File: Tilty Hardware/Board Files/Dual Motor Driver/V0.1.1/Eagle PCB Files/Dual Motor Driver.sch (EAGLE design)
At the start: 33 parts, among them J1 AVR_SPI_PRG_6PTH, Q1 16MHz, U1 ATMEGA328P, U2 L298_BRIDGE_DRIVER, U5 VOLTAGE-REGULATOR

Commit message: Tilty PCB work
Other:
- note added: "headers need to be updated!"
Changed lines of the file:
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@@
 <text x="2.54" y="5.08" size="1.778" layer="91">Change to a non-
 Sparkfun button</text>
+<text x="182.88" y="40.64" size="2.54" layer="91" ratio="15">headers need to be updated!</text>
 </plain>
 <instances>

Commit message: Finished Tilty Duo/Quad 0.2.4, work on motor driver
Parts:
- removed JP8: (no value), SparkFun-Connectors:M063.5MM-6
- removed JP9: (no value), pinhead:PINHD-2X3/90
- removed U5: VOLTAGE-REGULATOR, My Parts:VOLTAGE-REGULATOR
- added U3: LM2931, on-semiconductor:LM2931
- C6: value 0.1uF -> 4.7uF
- C7: value 1uF -> 0.1uF
- JP7: value (none) -> 2-POS_SMD_TERM_BLOCK; device pinhead:PINHD-2X3/90 -> My Parts:2-POS_SMD_TERM_BLOCK
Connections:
- net +24V: now also JP7.1, U3.VIN; no longer JP8.4, U5.VIN
- net +5V: now also U3.5V; no longer U5.VOUT
- net ENC1B: now also U1.PC1(ADC1)
- net ENC2A: now also JP5.3, U1.PC0(ADC0); no longer JP5.4, U1.PD3(INT1)
- net ENC2B: now also JP5.4, U1.PD3(INT1); no longer JP5.3
- net GND: now also JP7.2, U3.GND; no longer JP8.3, U5.GND
- net M1A: now also JP6.2; no longer JP6.1, JP8.6
- net M1B: now also JP6.1; no longer JP6.2, JP8.5
- net M2A: now also JP5.6; no longer JP5.5, JP8.2
- net M2B: now also JP5.5; no longer JP5.6, JP8.1
- net SENSE_1: now also U1.PC2(ADC2); no longer U1.PC0(ADC0)
- net SENSE_2: now also U1.PC3(ADC3); no longer U1.PC1(ADC1)

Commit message: Nearly finalized dual motor driver add-on
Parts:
- added D10: (no value), SparkFun-LED:LED-GREENLED-0805_NO_SILK
- added D9: (no value), diode:DIODE-DO214AA
- added JP10, JP9: (no value), SparkFun-Connectors:M02PTH
- added JP8: (no value), SparkFun-Connectors:M04LOCK
- added R6: (no value), resistor:R-US_R0603
- added SJ2: SOLDERJUMPERTRACE, SparkFun-Passives:SOLDERJUMPERTRACE
- JP1, JP2, JP3, JP4: value (none) -> 8-PIN_HEADER; device pinhead:PINHD-1X81X08_NO_SILK -> My Parts:8-PIN_HEADER
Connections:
- new net N$1: D10.A, R6.2
- new net N$3: C7.1, D9.A, SJ2.1, U3.VIN
- new net RX: JP8.3, U1.PD0(RXD)
- new net TX: JP8.4, U1.PD1(TXD)
- net +24V: now also D9.C, SJ2.2; no longer C7.1, U3.VIN
- net +5V: now also JP8.1, R6.1
- net GND: now also D10.C, JP8.2, U2.GND@20
- net M1A: now also JP9.2
- net M1B: now also JP9.1
- net M2A: now also JP10.2
- net M2B: now also JP10.1
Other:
- note added: "Zener"
- note removed: "headers need to be updated!"

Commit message: New RC Receiver add-on testing code and minor motor driver updates
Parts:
- J1: value AVR_SPI_PRG_6PTH -> AVR_SPI_PRG_62X3_LOCK; device SparkFun-Connectors:AVR_SPI_PRG_6PTH -> SparkFun-Connectors:AVR_SPI_PRG_62X3_LOCK
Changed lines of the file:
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@@
 </part>
 <part name="P+4" library="supply1" deviceset="+24V" device=""/>
-<part name="J1" library="SparkFun-Connectors" deviceset="AVR_SPI_PRG_6" device="PTH"/>
+<part name="J1" library="SparkFun-Connectors" deviceset="AVR_SPI_PRG_6" device="2X3_LOCK" value="AVR_SPI_PRG_62X3_LOCK"/>
 <part name="GND6" library="supply1" deviceset="GND" device=""/>
 <part name="P+5" library="supply1" deviceset="+5V" device=""/>

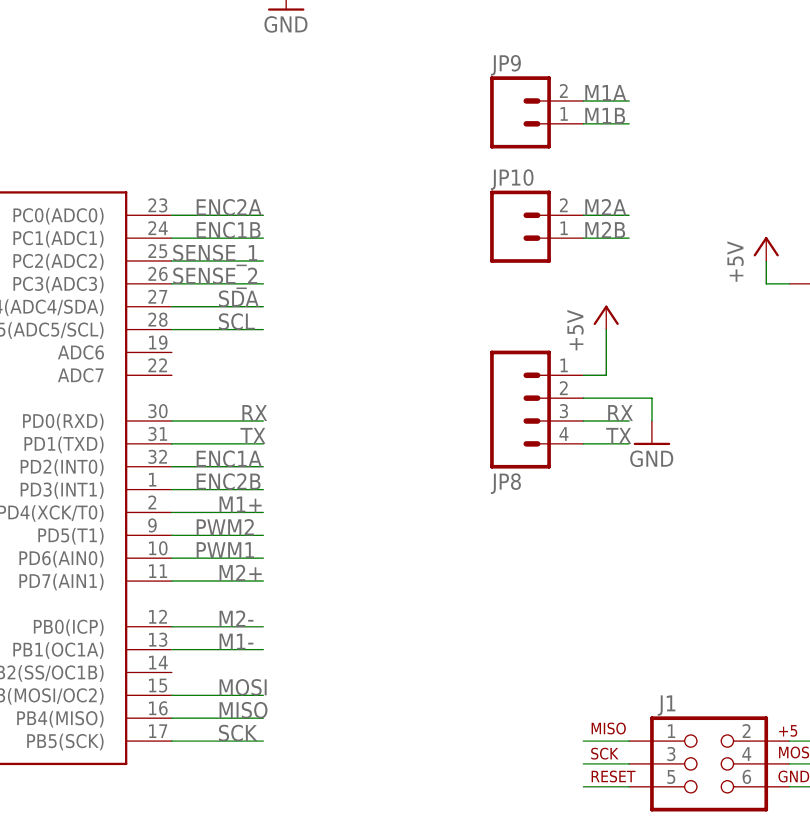
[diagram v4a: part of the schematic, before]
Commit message: Motor driver: added test code, updated things.todo, some hardware updates
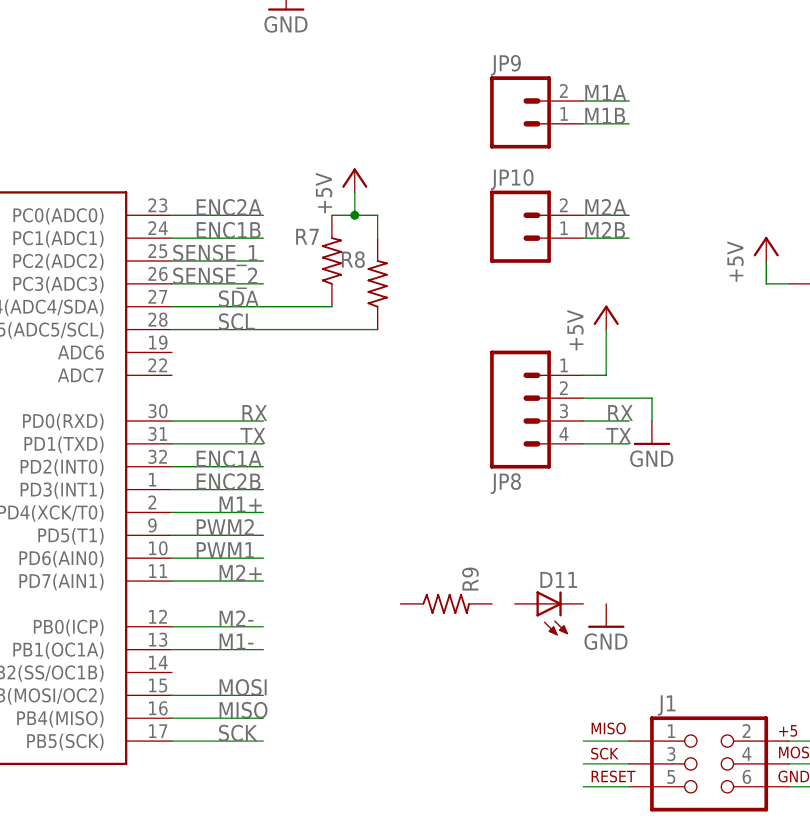
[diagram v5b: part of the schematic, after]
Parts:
- added D11: (no value), SparkFun-LED:LED-GREENLED-0805_NO_SILK
- added R7, R8, R9: (no value), resistor:R-US_R0603
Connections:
- net +5V: now also R7.2, R8.2
- net SCL: now also R8.1
- net SDA: now also R7.1
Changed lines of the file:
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@@
 <part name="P+13" library="supply1" deviceset="+5V" device=""/>
 <part name="GND16" library="supply1" deviceset="GND" device=""/>
+<part name="R7" library="resistor" deviceset="R-US_" device="R0603"/>
+<part name="R8" library="resistor" deviceset="R-US_" device="R0603"/>
+<part name="P+14" library="supply1" deviceset="+5V" device=""/>
+<part name="R9" library="resistor" deviceset="R-US_" device="R0603"/>
+<part name="D11" library="SparkFun-LED" deviceset="LED-GREEN" device="LED-0805_NO_SILK"/>
+<part name="GND17" library="supply1" deviceset="GND" device=""/>
 </parts>
 <sheets>
@@
 <instance part="P+13" gate="1" x="167.64" y="63.5"/>
 <instance part="GND16" gate="1" x="190.5" y="53.34"/>
+<instance part="R7" gate="G$1" x="119.38" y="60.96" smashed="yes" rot="R90">
+<attribute name="NAME" x="118.11" y="64.5414" size="1.778" layer="95" rot="R180"/>
+<attribute name="VALUE" x="118.11" y="61.722" size="1.778" layer="96" rot="R180"/>
+</instance>
+<instance part="R8" gate="G$1" x="124.46" y="58.42" smashed="yes" rot="R90">
+<attribute name="NAME" x="123.19" y="62.0014" size="1.778" layer="95" rot="R180"/>
+<attribute name="VALUE" x="123.19" y="59.182" size="1.778" layer="96" rot="R180"/>
+</instance>
+<instance part="P+14" gate="1" x="121.92" y="71.12"/>
+<instance part="R9" gate="G$1" x="132.08" y="22.86" smashed="yes">
+<attribute name="NAME" x="135.6614" y="24.13" size="1.778" layer="95" rot="R90"/>
+<attribute name="VALUE" x="132.842" y="24.13" size="1.778" layer="96" rot="R90"/>
+</instance>
+<instance part="D11" gate="G$1" x="142.24" y="22.86" rot="R90"/>
+<instance part="GND17" gate="1" x="149.86" y="20.32"/>
 </instances>
 <busses>
@@
 <wire x1="167.64" y1="58.42" x2="170.18" y2="58.42" width="0.1524" layer="91"/>
 </segment>
+<segment>
+<pinref part="R7" gate="G$1" pin="2"/>
+<pinref part="R8" gate="G$1" pin="2"/>
+<wire x1="119.38" y1="66.04" x2="121.92" y2="66.04" width="0.1524" layer="91"/>
+<wire x1="121.92" y1="66.04" x2="124.46" y2="66.04" width="0.1524" layer="91"/>
+<wire x1="124.46" y1="66.04" x2="124.46" y2="63.5" width="0.1524" layer="91"/>
+<pinref part="P+14" gate="1" pin="+5V"/>
+<wire x1="121.92" y1="68.58" x2="121.92" y2="66.04" width="0.1524" layer="91"/>
+<junction x="121.92" y="66.04"/>
+</segment>
 </net>
 <net name="RESET" class="0">
@@
 <segment>
 <pinref part="U1" gate="G$1" pin="PC4(ADC4/SDA)"/>
-<wire x1="101.6" y1="55.88" x2="111.76" y2="55.88" width="0.1524" layer="91"/>
+<wire x1="101.6" y1="55.88" x2="119.38" y2="55.88" width="0.1524" layer="91"/>
 <label x="106.68" y="55.88" size="1.778" layer="95"/>
+<pinref part="R7" gate="G$1" pin="1"/>
 </segment>
 </net>
@@
 <segment>
 <pinref part="U1" gate="G$1" pin="PC5(ADC5/SCL)"/>
-<wire x1="101.6" y1="53.34" x2="111.76" y2="53.34" width="0.1524" layer="91"/>
 <label x="106.68" y="53.34" size="1.778" layer="95"/>
-</segment>
-</net>
+<pinref part="R8" gate="G$1" pin="1"/>
+<wire x1="101.6" y1="53.34" x2="124.46" y2="53.34" width="0.1524" layer="91"/>
+</segment>
+</net>

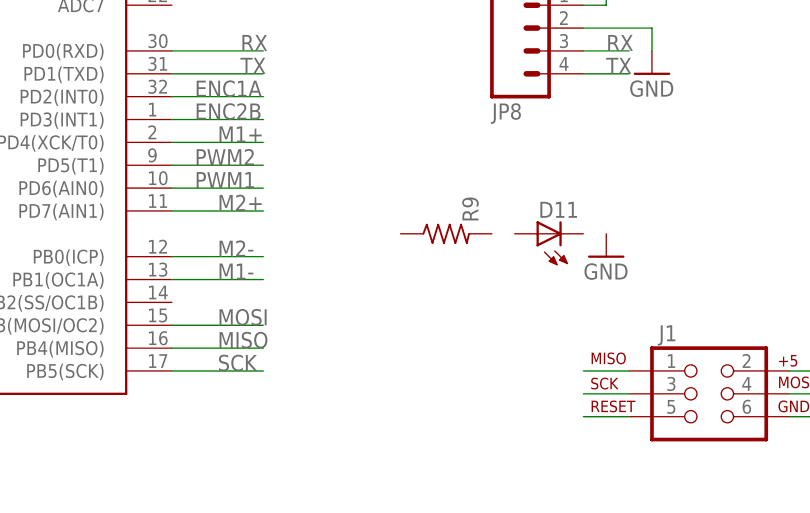
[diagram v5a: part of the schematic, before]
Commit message: Changes to Dual Motor Driver add-on
Moved some res and caps around.
Added a status LED.
Added silkscreen to rectifier diodes to show orientations.
Added I2C pullup resistors.
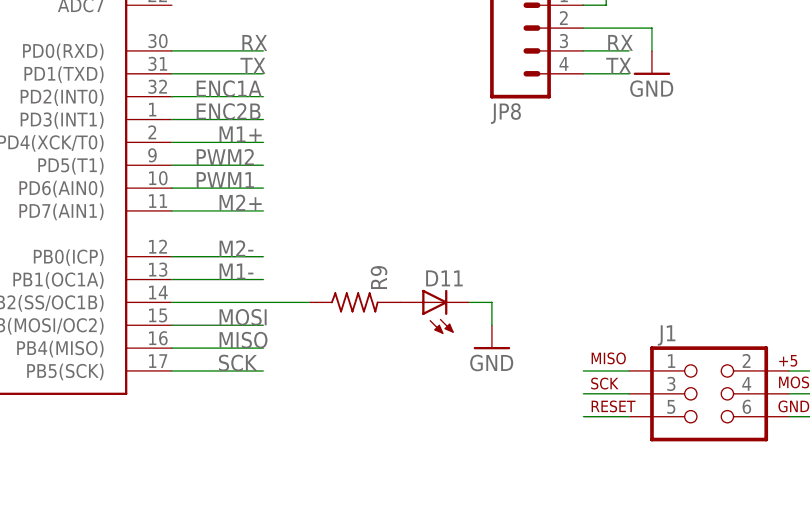
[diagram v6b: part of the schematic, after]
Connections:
- new net N$2: D11.A, R9.2
- new net N$4: R9.1, U1.PB2(SS/OC1B)
- net GND: now also D11.C
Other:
- moved on the sheet: D11, R9
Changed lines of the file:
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@@
 </instance>
 <instance part="P+14" gate="1" x="121.92" y="71.12"/>
-<instance part="R9" gate="G$1" x="132.08" y="22.86" smashed="yes">
-<attribute name="NAME" x="135.6614" y="24.13" size="1.778" layer="95" rot="R90"/>
-<attribute name="VALUE" x="132.842" y="24.13" size="1.778" layer="96" rot="R90"/>
+<instance part="R9" gate="G$1" x="121.92" y="15.24" smashed="yes">
+<attribute name="NAME" x="125.5014" y="16.51" size="1.778" layer="95" rot="R90"/>
+<attribute name="VALUE" x="122.682" y="16.51" size="1.778" layer="96" rot="R90"/>
 </instance>
-<instance part="D11" gate="G$1" x="142.24" y="22.86" rot="R90"/>
-<instance part="GND17" gate="1" x="149.86" y="20.32"/>
+<instance part="D11" gate="G$1" x="129.54" y="15.24" rot="R90"/>
+<instance part="GND17" gate="1" x="137.16" y="10.16"/>
 </instances>
 <busses>
@@
 <wire x1="190.5" y1="58.42" x2="190.5" y2="55.88" width="0.1524" layer="91"/>
 </segment>
+<segment>
+<pinref part="D11" gate="G$1" pin="C"/>
+<pinref part="GND17" gate="1" pin="GND"/>
+<wire x1="134.62" y1="15.24" x2="137.16" y2="15.24" width="0.1524" layer="91"/>
+<wire x1="137.16" y1="15.24" x2="137.16" y2="12.7" width="0.1524" layer="91"/>
+</segment>
 </net>
 <net name="M1A" class="0">
@@
 </segment>
 </net>
+<net name="N$2" class="0">
+<segment>
+<pinref part="R9" gate="G$1" pin="2"/>
+<pinref part="D11" gate="G$1" pin="A"/>
+</segment>
+</net>
+<net name="N$4" class="0">
+<segment>
+<pinref part="U1" gate="G$1" pin="PB2(SS/OC1B)"/>
+<pinref part="R9" gate="G$1" pin="1"/>
+<wire x1="101.6" y1="15.24" x2="116.84" y2="15.24" width="0.1524" layer="91"/>
+</segment>
+</net>
